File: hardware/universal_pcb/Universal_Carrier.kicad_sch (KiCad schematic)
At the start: 22 parts, among them J1 ESP32_T_LANDSCAPE, J10 RACK_CREMALHEIRA, J11 PWR_ESP_5V, J12 PWR_SERVO_5V, J2 ESP32_B_LANDSCAPE, J3 SX1278_LORA_2x4, J4 BATT_APM, J5 BUZZER, J6 GPS_LC29H_7PIN, J7 ESC_PROP_UP, J8 RUDDER_DN, J9 WINCH_MODE, SW1 UP, SW2 MODE, SW3 DOWN, SW4 BOOT

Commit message: feat: add new universal PCB gerbers, logos, and updated design files
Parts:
- removed JP_RBL: REMOVE_BEFORE_LAUNCH, Connector_PinHeader_2.54mm:PinHeader_1x04_P2.54mm_Vertical, symbol Connector_Generic:Conn_01x04
- J4: value BATT_APM -> APM_JOY; footprint Connector_PinHeader_2.54mm:PinHeader_1x03_P2.54mm_Horizontal -> Connector_PinHeader_2.54mm:PinHeader_1x04_P2.54mm_Vertical; symbol Connector_Generic:Conn_01x03 -> Connector_Generic:Conn_01x04
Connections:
- net JOY_X is gone; now on net IO0_ADC: JOY1.H2 (H2_ADC)
- net JOY_Y is gone; now on net IO1_ADC: JOY1.V2 (V2_ADC)
- net +3V3: now also J4.4 (Pin_4)
- net GND: now also SW4.1; no longer SW4.2
- net IO9_BOOT: now also SW4.2; no longer SW4.1

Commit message: feat: update PCB gerber files and add logo bitmap header
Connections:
- net IO16_GPS_RX: now also J6.5 (Pin_5); no longer J6.4 (Pin_4)
- net IO17_GPS_TX: now also J6.4 (Pin_4); no longer J6.5 (Pin_5)
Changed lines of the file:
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@@
-	(wire
-		(pts
-			(xy 213.36 137.16) (xy 200.66 137.16)
-		)
-		(stroke
-			(width 0)
-			(type solid)
-		)
-	)
 	(wire
 		(pts
@@
 	(wire
 		(pts
-			(xy 213.36 139.7) (xy 200.66 139.7)
-		)
-		(stroke
-			(width 0)
-			(type solid)
-		)
-	)
-	(wire
-		(pts
 			(xy 109.22 163.83) (xy 96.52 163.83)
 		)
@@
 	(wire
 		(pts
+			(xy 200.66 137.16) (xy 213.36 137.16)
+		)
+		(stroke
+			(width 0)
+			(type default)
+		)
+	)
+	(wire
+		(pts
 			(xy 45.72 71.12) (xy 33.02 71.12)
 		)
@@
 		(pts
 			(xy 147.32 137.16) (xy 142.24 137.16)
+		)
+		(stroke
+			(width 0)
+			(type default)
+		)
+	)
+	(wire
+		(pts
+			(xy 200.66 139.7) (xy 213.36 139.7)
 		)
 		(stroke
@@
 	)
 	(label "IO16_GPS_RX"
-		(at 200.66 137.16 180)
+		(at 200.66 139.7 180)
 		(effects
 			(font
@@
 	)
 	(label "IO17_GPS_TX"
-		(at 200.66 139.7 180)
-		(effects
-			(font
+		(at 200.66 137.16 180)
+		(effects
+			(font

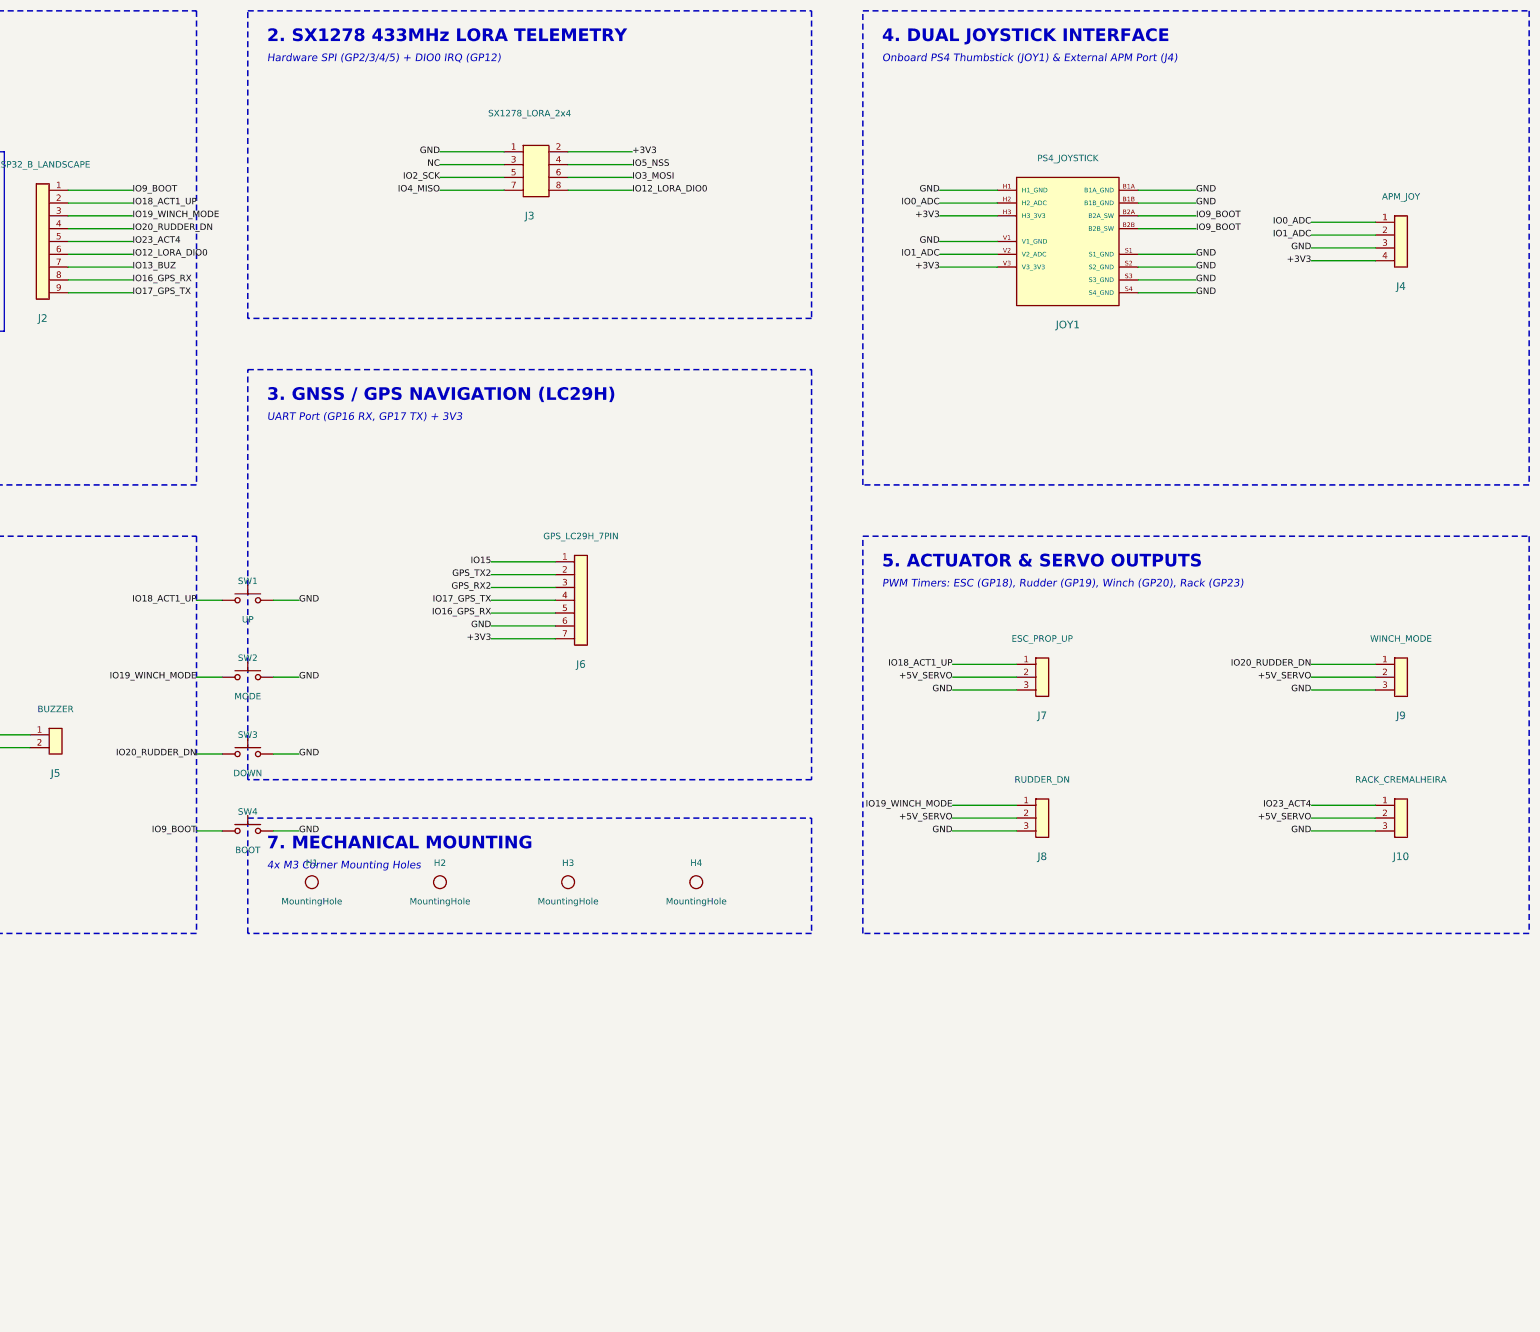
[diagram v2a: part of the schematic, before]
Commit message: feat: add hardware joystick testing page and update universal carrier PCB and gerber files
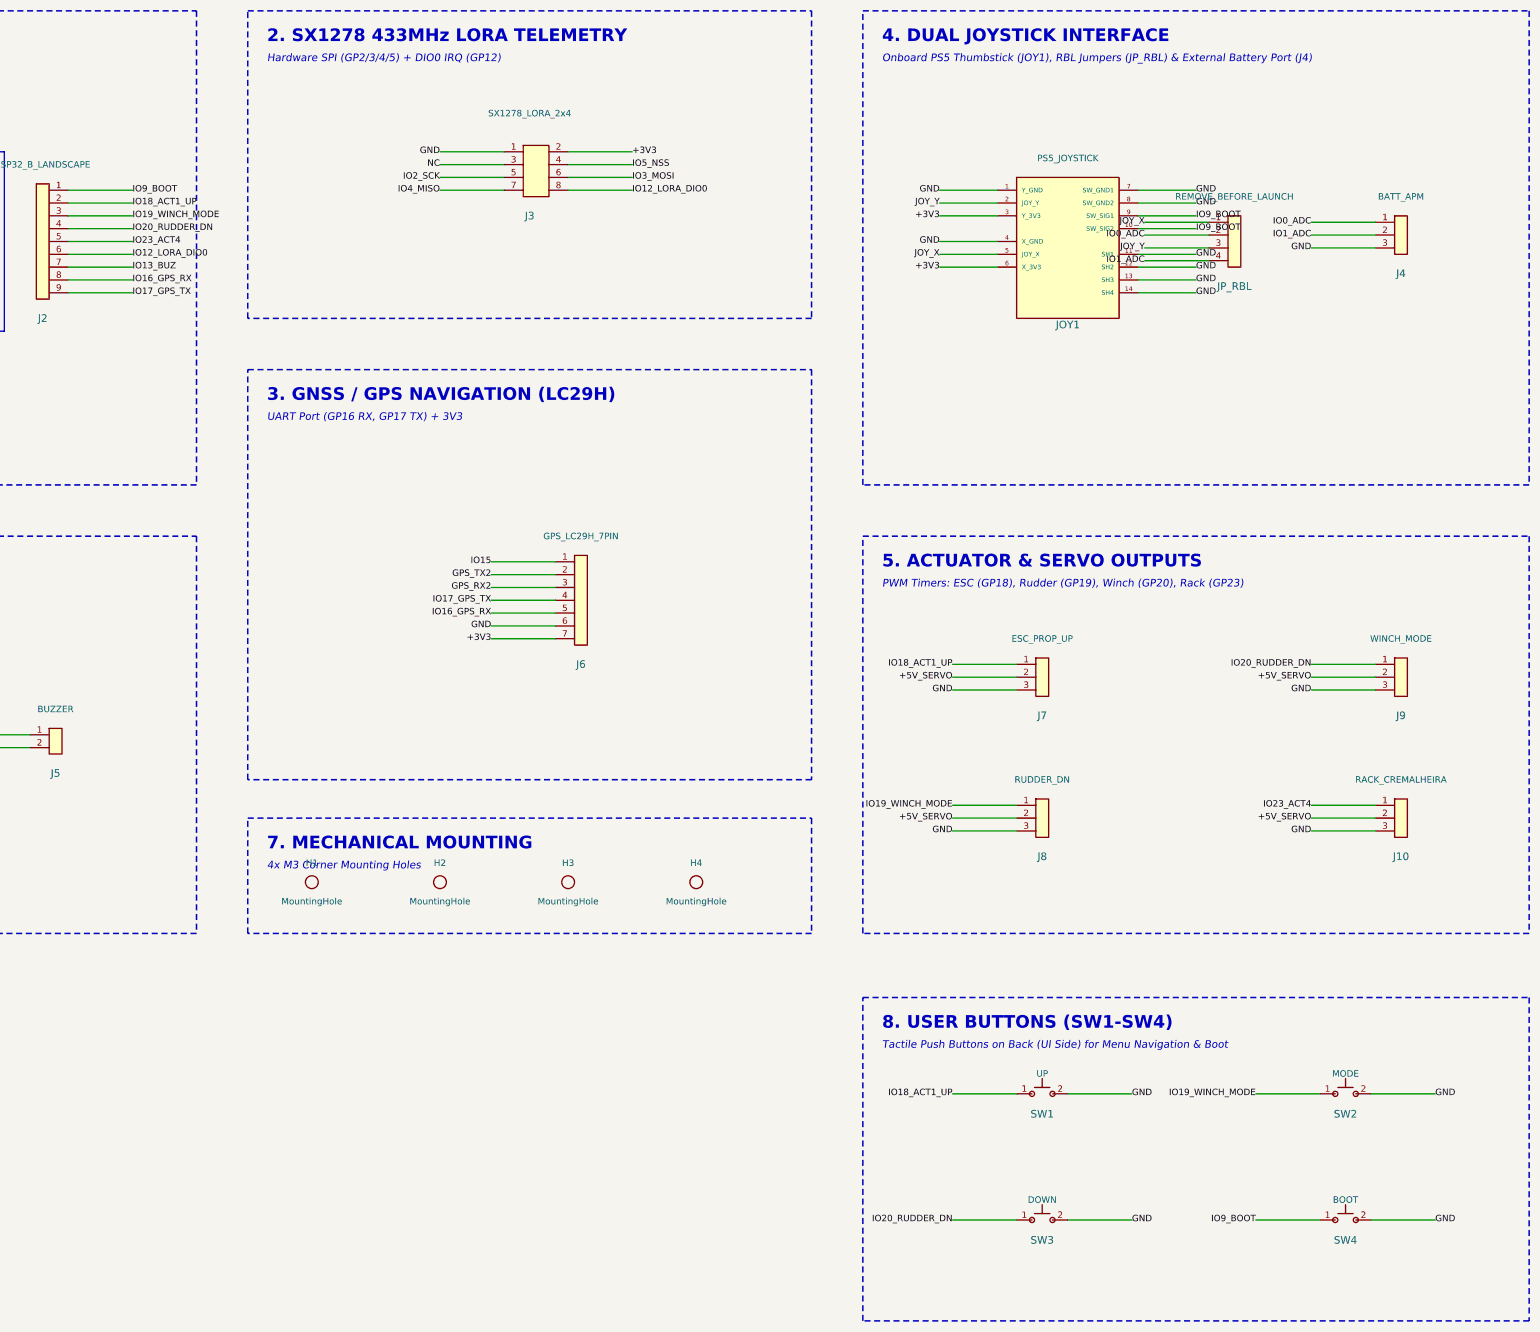
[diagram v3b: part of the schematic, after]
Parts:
- removed J4: APM_JOY, Connector_PinHeader_2.54mm:PinHeader_1x04_P2.54mm_Vertical, symbol Connector_Generic:Conn_01x04
- removed JOY1: PS4_JOYSTICK, PS4_joystick:XDCR_COM-09032, symbol Device:Joystick_PS4_Thumbstick
- added J4: BATT_APM, Connector_PinHeader_2.54mm:PinHeader_1x03_P2.54mm_Horizontal, symbol Connector_Generic:Conn_01x03
- added JOY1: PS5_JOYSTICK, PS5_joystick:Alps_RKJXV1224005, symbol Device:Joystick_PS5_Thumbstick
- added JP_RBL: REMOVE_BEFORE_LAUNCH, Connector_PinHeader_2.54mm:PinHeader_1x04_P2.54mm_Vertical, symbol Connector_Generic:Conn_01x04
- J6: footprint Connector_PinHeader_2.54mm:PinHeader_1x07_P2.54mm_Vertical -> Connector_PinHeader_2.54mm:PinHeader_1x07_P2.54mm_Horizontal
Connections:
- net +3V3: now also JOY1.3 (Y_3V3), JOY1.6 (X_3V3)
- net GND: now also SW4.2, J4.3 (Pin_3), JOY1.1 (Y_GND), JOY1.11 (SH1), JOY1.12 (SH2), JOY1.13 (SH3), JOY1.14 (SH4), JOY1.4 (X_GND), JOY1.7 (SW_GND1), JOY1.8 (SW_GND2); no longer SW4.1
- net IO0_ADC: now also J4.1 (Pin_1), JP_RBL.2 (Pin_2)
- net IO1_ADC: now also J4.2 (Pin_2), JP_RBL.4 (Pin_4)
- net IO9_BOOT: now also SW4.1, JOY1.10 (SW_SIG2), JOY1.9 (SW_SIG1); no longer SW4.2
- new net JOY_X: JOY1.5 (JOY_X), JP_RBL.1 (Pin_1)
- new net JOY_Y: JOY1.2 (JOY_Y), JP_RBL.3 (Pin_3)
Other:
- note added: "8. USER BUTTONS (SW1-SW4)"
- note added: "Onboard PS5 Thumbstick (JOY1), RBL Jumpers (JP_RBL) & External Battery Port (J4)"
- note added: "Tactile Push Buttons on Back (UI Side) for Menu Navigation & Boot"
- note removed: "Onboard PS4 Thumbstick (JOY1) & External APM Port (J4)"

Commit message: feat: update Universal Carrier PCB design and hardware configurations for I2C support
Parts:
- removed J10: RACK_CREMALHEIRA, Connector_PinHeader_2.54mm:PinHeader_1x03_P2.54mm_Horizontal, symbol Connector_Generic:Conn_01x03
- removed J7: ESC_PROP_UP, Connector_PinHeader_2.54mm:PinHeader_1x03_P2.54mm_Horizontal, symbol Connector_Generic:Conn_01x03
- removed J8: RUDDER_DN, Connector_PinHeader_2.54mm:PinHeader_1x03_P2.54mm_Horizontal, symbol Connector_Generic:Conn_01x03
- removed J9: WINCH_MODE, Connector_PinHeader_2.54mm:PinHeader_1x03_P2.54mm_Horizontal, symbol Connector_Generic:Conn_01x03
- removed JP_RBL: REMOVE_BEFORE_LAUNCH, Connector_PinHeader_2.54mm:PinHeader_1x04_P2.54mm_Vertical, symbol Connector_Generic:Conn_01x04
- added J_ADS: ADS1115_MODULE, Connector_PinHeader_2.54mm:PinHeader_1x10_P2.54mm_Horizontal, symbol Connector_Generic:Conn_01x10
- added J_PCA_IN: PCA9685_INPUT, Connector_PinHeader_2.54mm:PinHeader_1x06_P2.54mm_Vertical, symbol Connector_Generic:Conn_01x06
- added J_PCA_OUT: PCA9685_CASCADE, Connector_PinHeader_2.54mm:PinHeader_1x06_P2.54mm_Vertical, symbol Connector_Generic:Conn_01x06
- J5: value BUZZER -> DETECTOR_ANCORA
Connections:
- net +3V3: now also J1.3 (Pin_3), J3.6 (Pin_6), J6.1 (Pin_1), J_ADS.10 (Pin_10), J_PCA_IN.2 (Pin_2); no longer J1.7 (Pin_7), J3.2 (Pin_2), J6.7 (Pin_7)
- net +5V: now also J1.1 (Pin_1), J11.1 (Pin_1); no longer J1.9 (Pin_9), J11.2 (Pin_2)
- net +5V_SERVO: now also J12.1 (Pin_1), J_PCA_IN.1 (Pin_1); no longer J12.2 (Pin_2)
- net GND: now also J1.2 (Pin_2), J11.2 (Pin_2), J12.2 (Pin_2), J3.5 (Pin_5), J4.1 (Pin_1), J5.1 (Pin_1), J6.2 (Pin_2), JOY1.10 (SW_BOOT2), JOY1.9 (SW_BOOT1), J_ADS.6 (Pin_6), J_ADS.9 (Pin_9), J_PCA_IN.5 (Pin_5), J_PCA_IN.6 (Pin_6); no longer J1.8 (Pin_8), J11.1 (Pin_1), J12.1 (Pin_1), J3.1 (Pin_1), J4.3 (Pin_3), J5.2 (Pin_2), J6.6 (Pin_6), JOY1.1 (Y_GND), JOY1.11 (SH1), JOY1.12 (SH2)
- net GPS_RX2: now also J6.5 (Pin_5); no longer J6.3 (Pin_3)
- net GPS_TX2: now also J6.6 (Pin_6); no longer J6.2 (Pin_2)
- net IO12_LORA_DIO0: now also J2.4 (Pin_4); no longer J2.6 (Pin_6), J3.8 (Pin_8)
- net IO15: now also J6.7 (Pin_7); no longer J6.1 (Pin_1)
- net IO16_GPS_RX: now also J2.2 (Pin_2), J6.3 (Pin_3); no longer J2.8 (Pin_8), J6.5 (Pin_5)
- net IO17_GPS_TX: now also J2.1 (Pin_1); no longer J2.9 (Pin_9)
- net IO2_SCK: now also J1.6 (Pin_6), J3.1 (Pin_1); no longer J1.4 (Pin_4), J3.5 (Pin_5)
- net IO3_MOSI: now also J1.7 (Pin_7), J3.2 (Pin_2); no longer J1.3 (Pin_3), J3.6 (Pin_6)
- net IO4_MISO: now also J1.8 (Pin_8); no longer J1.2 (Pin_2), J3.7 (Pin_7)
- net IO5_NSS: now also J1.9 (Pin_9); no longer J1.1 (Pin_1)
- net IO9_BOOT: now also J2.9 (Pin_9), JOY1.11 (SHIELD1), JOY1.12 (SHIELD2); no longer J2.1 (Pin_1), JOY1.10 (SW_SIG2), JOY1.9 (SW_SIG1)
- net JOY_X: no longer JOY1.5 (JOY_X)
- net JOY_Y: no longer JOY1.2 (JOY_Y)
- net NC: now also J_ADS.5 (Pin_5)
- removed net IO0_ADC: J1.6 (Pin_6), J4.1 (Pin_1)
- net IO13_BUZ renamed IO19_MODE
- net IO19_MODE: now also SW2.1; no longer J5.1 (Pin_1)
- net IO18_ACT1_UP renamed IO18_UP
- net IO18_UP: now also J2.8 (Pin_8); no longer J2.2 (Pin_2)
- net IO19_WINCH_MODE renamed IO13_ANCORA_DET
- net IO13_ANCORA_DET: now also J5.2 (Pin_2); no longer SW2.1
- net IO1_ADC renamed BATT_CURR_APM
- net BATT_CURR_APM: now also J_ADS.3 (Pin_3); no longer J1.5 (Pin_5)
- net IO20_RUDDER_DN renamed IO20_DN
- net IO20_DN: now also J2.6 (Pin_6); no longer J2.4 (Pin_4)
- net IO23_ACT4 renamed IO23_SPARE
- new net AUX_ADC: J_ADS.1 (Pin_1)
- new net BATT_VOLT_APM: J4.3 (Pin_3), J_ADS.4 (Pin_4)
- new net I2C_SCL: J1.5 (Pin_5), J_ADS.8 (Pin_8), J_PCA_IN.4 (Pin_4)
- new net I2C_SDA: J1.4 (Pin_4), J_ADS.7 (Pin_7), J_PCA_IN.3 (Pin_3)
- new net WATER_SENS: J_ADS.2 (Pin_2)
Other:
- note added: "16 Hardware Servos: Ch0 ESC, Ch1 Leme, Ch2 Guincho, Ch3 Rack, Ch4-15 LEDs"
- note added: "4. JOYSTICK & BATTERY INTERFACE"
- note added: "5. PCA9685 16-CH PWM CONTROLLER (I2C: 0x40)"
- note added: "6. POWER & SENSOR DISTRIBUTION"
- note added: "9. ADS1115 16-BIT 4-CH ADC (I2C: 0x48)"
- note added: "CH0: ESC Propulsão | CH1: Servo Leme | CH2: Guincho Âncora"
- note added: "CH3: Cremalheira Âncora | CH4-15: LEDs, Faróis de Navegação e Auxiliares"
- note added: "Dual 1x09 Headers (J1 Top / SPI & I2C, J2 Bottom / UART & Signals)"
- note added: "High Precision Telemetry: A0 V_Batt, A1 I_Batt, A2 Water Sensor, A3 Aux"
- note added: "Isolated +5V Logic, +5V Servo Rail & Anchor End-Stop Sensor"
- note added: "Onboard PS5 Thumbstick (JOY1) & External Battery Port (J4)"
- note removed: "4. DUAL JOYSTICK INTERFACE"
- note removed: "5. ACTUATOR & SERVO OUTPUTS"
- note removed: "6. POWER & ALARM DISTRIBUTION"
- note removed: "Dual 1x09 Headers (J1 Top / SPI, J2 Bottom / Actuators & GPS)"
- note removed: "Isolated +5V Logic, +5V Servo Rail & Piezo Siren"
- note removed: "Onboard PS5 Thumbstick (JOY1), RBL Jumpers (JP_RBL) & External Battery Port (J4)"
- note removed: "PWM Timers: ESC (GP18), Rudder (GP19), Winch (GP20), Rack (GP23)"
